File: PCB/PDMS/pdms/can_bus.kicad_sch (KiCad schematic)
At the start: 8 parts, among them U2 MCP2561-E-SN, U3 MCP2561-E-SN

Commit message: Flash layout
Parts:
- C64, C65: footprint Capacitor_SMD:C_0402_1005Metric_Pad0.74x0.62mm_HandSolder -> Capacitor_SMD:C_0402_1005Metric
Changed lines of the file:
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@@
     (property "Reference" "C64" (id 0) (at 50.292 22.225 90))
     (property "Value" "100nF" (id 1) (at 51.562 28.575 90))
-    (property "Footprint" "Capacitor_SMD:C_0402_1005Metric_Pad0.74x0.62mm_HandSolder" (id 2) (at 50.292 25.4 0)
+    (property "Footprint" "Capacitor_SMD:C_0402_1005Metric" (id 2) (at 50.292 25.4 0)
       (effects (font (size 1.27 1.27)) hide)
     )
@@
     (property "Reference" "C65" (id 0) (at 50.292 82.677 90))
     (property "Value" "100nF" (id 1) (at 51.562 89.027 90))
-    (property "Footprint" "Capacitor_SMD:C_0402_1005Metric_Pad0.74x0.62mm_HandSolder" (id 2) (at 50.292 85.852 0)
+    (property "Footprint" "Capacitor_SMD:C_0402_1005Metric" (id 2) (at 50.292 85.852 0)
       (effects (font (size 1.27 1.27)) hide)
     )

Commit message: Major changes with new switch
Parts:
- added C87: 100nF, Capacitor_SMD:C_0805_2012Metric, symbol Device:C_Small
- added IC17: TS5A21366DCUR, PDM_Additional:SOP50P310X90-8N, symbol PDM_additional:TS5A21366DCUR
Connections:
- net CAN1_H: now also IC17.2 (COM1); no longer R58.1
- net CAN1_L: now also R58.1; no longer R58.2
- net CAN2_H: now also IC17.6 (COM2); no longer R59.2
- net GND: now also C87.1, IC17.4 (GND)
- new net: IC17.1 (NO1), R58.2
- new net: IC17.5 (NO2), R59.2
- new net +3.3V: C87.2, IC17.8 (V+)
- new net CAN_TERMINATOR_1: IC17.7 (IN1)
- new net CAN_TERMINATOR_2: IC17.3 (IN2)

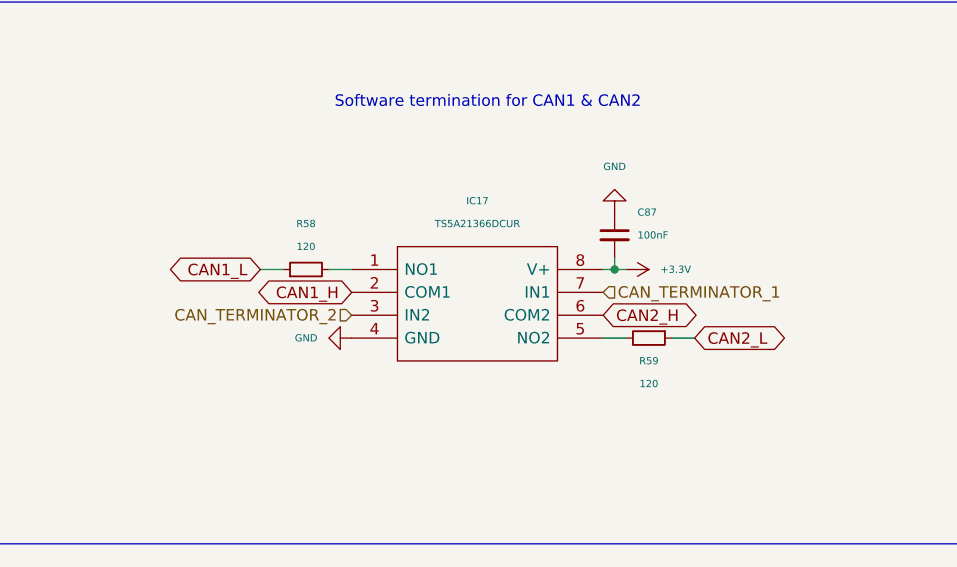
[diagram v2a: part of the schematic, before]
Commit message: Added can-bus software switching and major changes in layout
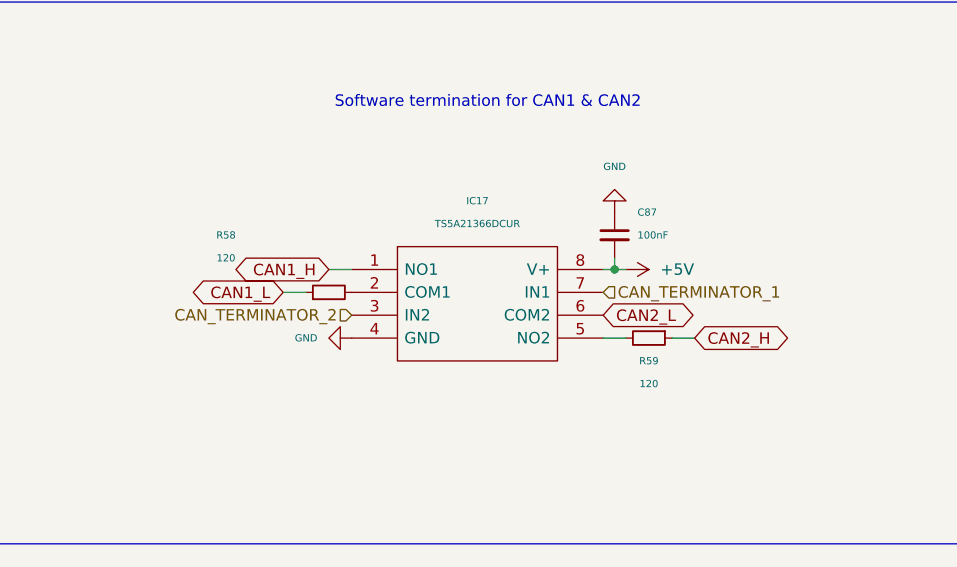
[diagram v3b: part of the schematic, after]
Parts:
- C87: footprint Capacitor_SMD:C_0805_2012Metric -> Capacitor_SMD:C_0402_1005Metric
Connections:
- net +3.3V is gone; now on net +5V: C87.2, IC17.8 (V+)
- net CAN1_H: now also IC17.1 (NO1); no longer IC17.2 (COM1)
- net CAN2_H: now also R59.1; no longer IC17.6 (COM2)
- net CAN2_L: now also IC17.6 (COM2); no longer R59.1
- net at R58.2: now also IC17.2 (COM1); no longer IC17.1 (NO1)
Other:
- moved on the sheet: R58
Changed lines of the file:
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@@
     (stroke (width 0) (type default) (color 0 0 0 0))
   )
-  (wire (pts (xy 119.38 41.91) (xy 121.92 41.91))
+  (wire (pts (xy 121.92 44.45) (xy 124.46 44.45))
     (stroke (width 0) (type default) (color 0 0 0 0))
   )
@@
     (effects (font (size 1.8 1.8)) (justify left bottom))
   )
-  (global_label "CAN1_L" (shape bidirectional) (at 119.38 41.91 180) (fields_autoplaced)
+  (global_label "CAN1_L" (shape bidirectional) (at 121.92 44.45 180) (fields_autoplaced)
     (effects (font (size 1.27 1.27)) (justify right))
-    (property "Intersheet References" "${INTERSHEET_REFS}" (id 0) (at 110.0726 41.8306 0)
+    (property "Intersheet References" "${INTERSHEET_REFS}" (id 0) (at 112.6126 44.3706 0)
       (effects (font (size 1.27 1.27)) (justify right) hide)
     )
   )
-  (global_label "CAN1_H" (shape bidirectional) (at 129.54 44.45 180) (fields_autoplaced)
+  (global_label "CAN1_H" (shape bidirectional) (at 127 41.91 180) (fields_autoplaced)
     (effects (font (size 1.27 1.27)) (justify right))
-    (property "Intersheet References" "${INTERSHEET_REFS}" (id 0) (at 119.9302 44.3706 0)
+    (property "Intersheet References" "${INTERSHEET_REFS}" (id 0) (at 117.3902 41.8306 0)
       (effects (font (size 1.27 1.27)) (justify right) hide)
     )
   )
-  (global_label "CAN2_H" (shape bidirectional) (at 157.48 46.99 0) (fields_autoplaced)
+  (global_label "CAN2_H" (shape bidirectional) (at 167.64 49.53 0) (fields_autoplaced)
     (effects (font (size 1.27 1.27)) (justify left))
-    (property "Intersheet References" "${INTERSHEET_REFS}" (id 0) (at 167.0898 46.9106 0)
+    (property "Intersheet References" "${INTERSHEET_REFS}" (id 0) (at 177.2498 49.4506 0)
       (effects (font (size 1.27 1.27)) (justify left) hide)
     )
@@
     )
   )
-  (global_label "CAN2_L" (shape bidirectional) (at 167.64 49.53 0) (fields_autoplaced)
+  (global_label "CAN2_L" (shape bidirectional) (at 157.48 46.99 0) (fields_autoplaced)
     (effects (font (size 1.27 1.27)) (justify left))
-    (property "Intersheet References" "${INTERSHEET_REFS}" (id 0) (at 176.9474 49.4506 0)
+    (property "Intersheet References" "${INTERSHEET_REFS}" (id 0) (at 166.7874 46.9106 0)
       (effects (font (size 1.27 1.27)) (justify left) hide)
     )
@@
     (pin "2")
   )
-  (symbol (lib_id "Device:R_Small") (at 124.46 41.91 90) (unit 1)
-    (in_bom yes) (on_board yes)
-    (property "Reference" "R58" (id 0) (at 124.46 36.83 90)
+  (symbol (lib_id "Device:R_Small") (at 127 44.45 90) (unit 1)
+    (in_bom yes) (on_board yes)
+    (property "Reference" "R58" (id 0) (at 115.57 38.1 90)
       (effects (font (size 0.8 0.8)))
     )
-    (property "Value" "120" (id 1) (at 124.46 39.37 90)
+    (property "Value" "120" (id 1) (at 115.57 40.64 90)
       (effects (font (size 0.8 0.8)))
     )
-    (property "Footprint" "Resistor_SMD:R_0402_1005Metric" (id 2) (at 124.46 41.91 0)
-      (effects (font (size 1.27 1.27)) hide)
-    )
-    (property "Datasheet" "~" (id 3) (at 124.46 41.91 0)
+    (property "Footprint" "Resistor_SMD:R_0402_1005Metric" (id 2) (at 127 44.45 0)
+      (effects (font (size 1.27 1.27)) hide)
+    )
+    (property "Datasheet" "~" (id 3) (at 127 44.45 0)
       (effects (font (size 1.27 1.27)) hide)
     )
@@
     (pin "1")
   )
-  (symbol (lib_id "power:+3.3V") (at 160.02 41.91 270) (unit 1)
-    (in_bom yes) (on_board yes) (fields_autoplaced)
-    (property "Reference" "#PWR0199" (id 0) (at 156.21 41.91 0)
-      (effects (font (size 0.8 0.8)) hide)
-    )
-    (property "Value" "+3.3V" (id 1) (at 163.83 41.9099 90)
-      (effects (font (size 0.8 0.8)) (justify left))
-    )
-    (property "Footprint" "" (id 2) (at 160.02 41.91 0)
-      (effects (font (size 1.27 1.27)) hide)
-    )
-    (property "Datasheet" "" (id 3) (at 160.02 41.91 0)
-      (effects (font (size 1.27 1.27)) hide)
-    )
-    (pin "1")
-  )
   (symbol (lib_id "Device:R_Small") (at 162.56 49.53 270) (unit 1)
     (in_bom yes) (on_board yes)
@@
       (effects (font (size 0.8 0.8)) (justify left))
     )
-    (property "Footprint" "Capacitor_SMD:C_0805_2012Metric" (id 2) (at 158.75 38.1 0)
+    (property "Footprint" "Capacitor_SMD:C_0402_1005Metric" (id 2) (at 158.75 38.1 0)
       (effects (font (size 1.27 1.27)) hide)
     )
@@
       (effects (font (size 1.27 1.27)) hide)
     )
+    (pin "1")
+  )
+  (symbol (lib_id "power:+5V") (at 160.02 41.91 270) (mirror x) (unit 1)
+    (in_bom yes) (on_board yes) (fields_autoplaced)
+    (property "Reference" "#PWR0117" (id 0) (at 156.21 41.91 0)
+      (effects (font (size 1.27 1.27)) hide)
+    )
+    (property "Value" "+5V" (id 1) (at 163.83 41.9099 90)
+      (effects (font (size 1.27 1.27)) (justify left))
+    )
+    (property "Footprint" "" (id 2) (at 160.02 41.91 0)
+      (effects (font (size 1.27 1.27)) hide)
+    )
+    (property "Datasheet" "" (id 3) (at 160.02 41.91 0)
+      (effects (font (size 1.27 1.27)) hide)
+    )

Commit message: Clean-up of schematics
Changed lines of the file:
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@@
     (stroke (width 0) (type default) (color 0 0 0 0))
   )
-  (text "CANBUS w/ software enabled termination" (at 99.695 128.27 0)
-    (effects (font (size 1.4 1.4)) (justify left bottom))
+  (text "CANBUS w/ software enabled termination" (at 99.441 129.032 0)
+    (effects (font (size 2 2)) (justify left bottom))
   )
   (text "CAN1" (at 16.51 20.32 0)

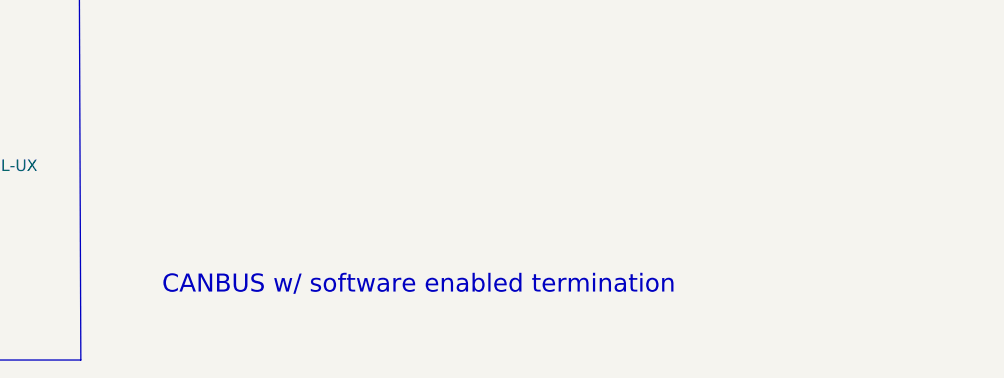
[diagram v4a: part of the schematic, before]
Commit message: WIP PCB folder structure and schematic clean-up
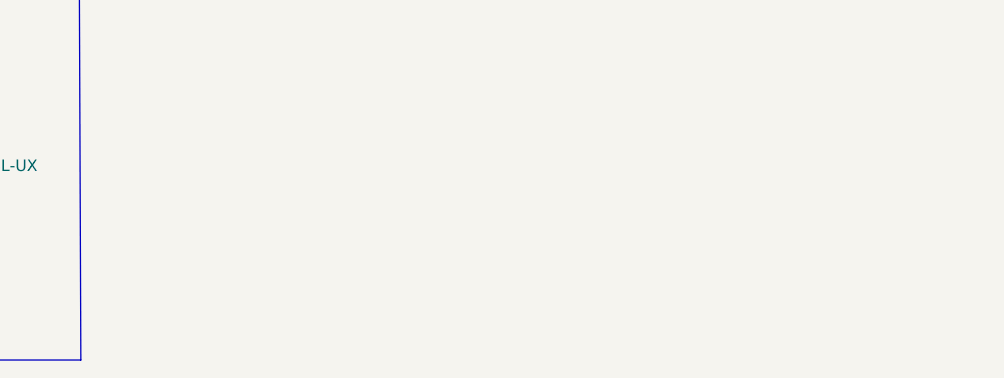
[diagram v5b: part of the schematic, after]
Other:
- note removed: "CANBUS w/ software enabled termination"
- company: (none) -> PGRacing Team
- title: (none) -> CANBUS w/ software enabled termination
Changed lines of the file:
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@@
 (kicad_sch (version 20211123) (generator eeschema)
   (paper "A5")
+  (title_block
+    (title "CANBUS w/ software enabled termination")
+    (rev "V4.2")
+    (company "PGRacing Team")
+    (comment 1 "Karol Pergoł")
+  )
   (junction (at 46.482 85.852) (diameter 0) (color 0 0 0 0)
   )
@@
     (stroke (width 0) (type default) (color 0 0 0 0))
   )
-  (text "CANBUS w/ software enabled termination" (at 99.441 129.032 0)
-    (effects (font (size 2 2)) (justify left bottom))
-  )
   (text "CAN1" (at 16.51 20.32 0)

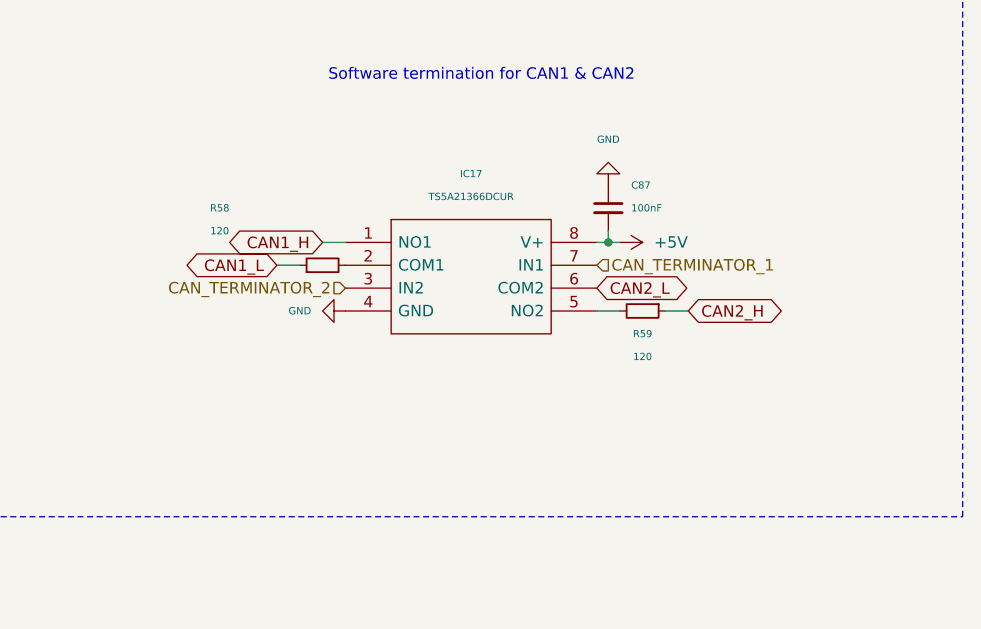
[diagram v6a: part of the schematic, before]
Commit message: Added gerbers of PDMS v4.3, assembly docs, modified DNP parameters
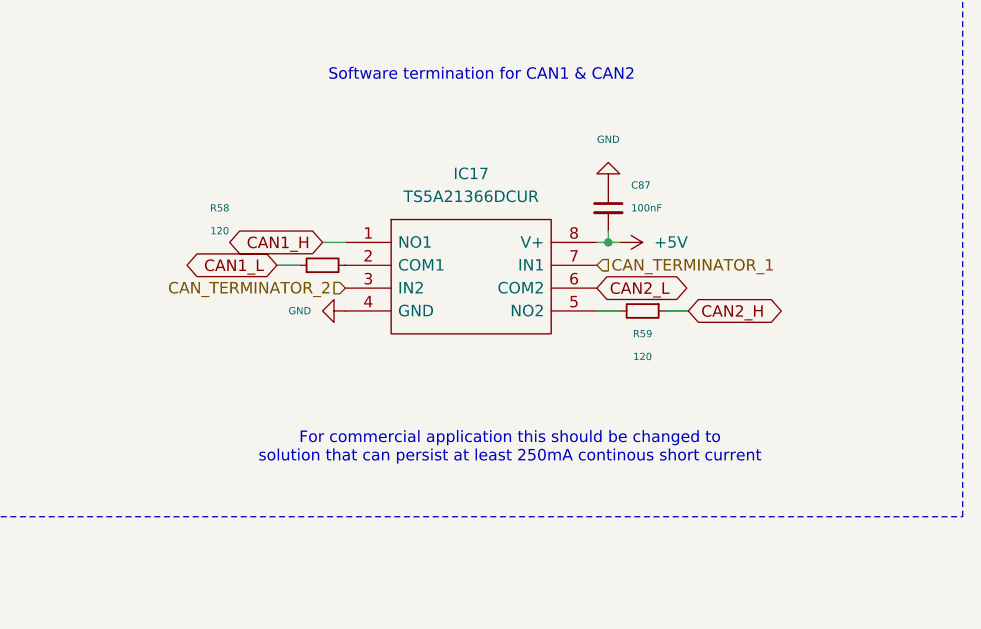
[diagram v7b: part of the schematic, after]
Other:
- note added: "For commercial application this should be changed to solution that can persist at least 250mA continous short current"
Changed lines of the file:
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@@
+		)
+	)
+	(text "For commercial application this should be changed to \nsolution that can persist at least 250mA continous short current"
+		(exclude_from_sim no)
+		(at 147.828 64.77 0)
+		(effects
+			(font
+				(size 1.27 1.27)
+			)
 		)
 	)
@@
 			(effects
 				(font
-					(size 0.8 0.8)
+					(size 1.27 1.27)
 				)
 			)
@@
 			(effects
 				(font
-					(size 0.8 0.8)
-				)
-			)
+					(size 1.27 1.27)
+				)
+			)
